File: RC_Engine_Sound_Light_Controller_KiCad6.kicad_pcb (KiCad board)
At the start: 2 copper layers, 87 x 40.3 mm, 44 parts, among them J1 RX, J10 RGB, J11 32, J12 CH1, J13 CH2, J14 CH3, J15 ESC, J16 CH4, J17 Brushed Motor output, J2 HeadL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

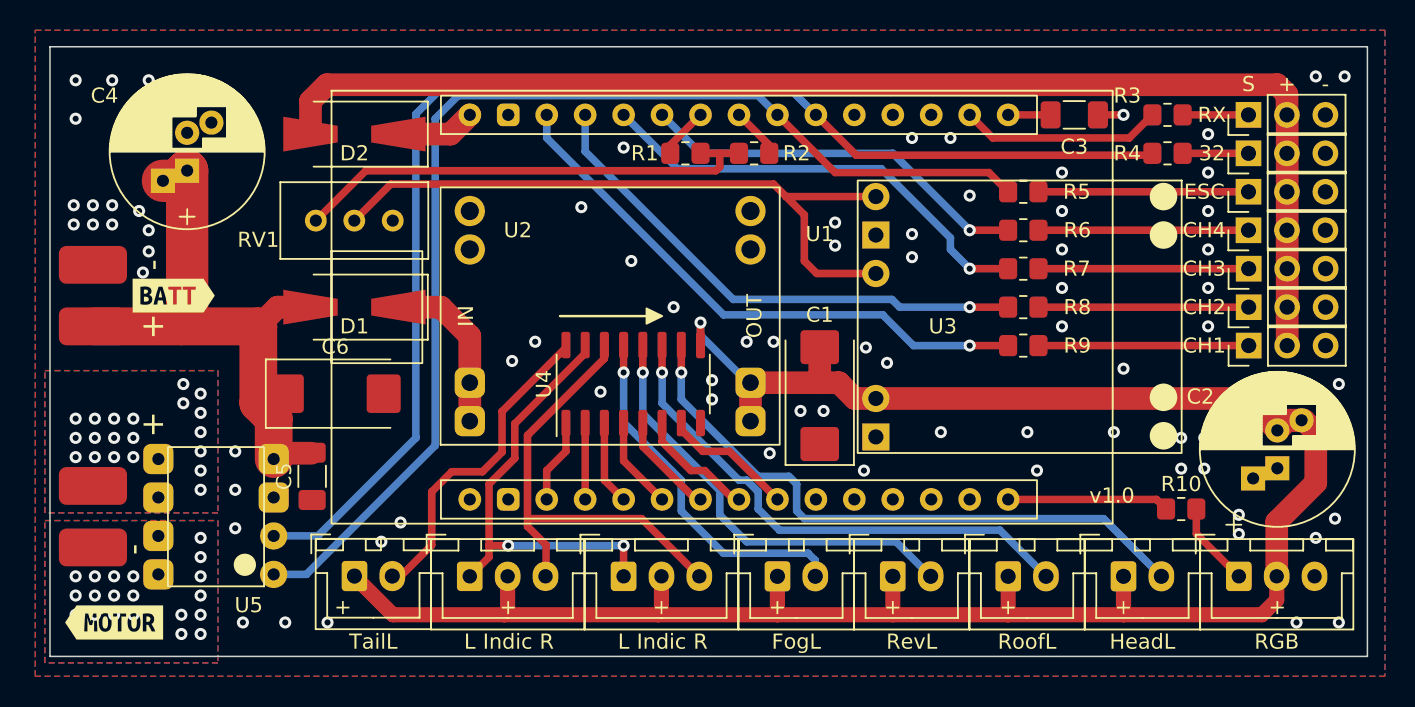
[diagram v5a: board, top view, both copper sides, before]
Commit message: Removed ESC and Pin 32 headers.
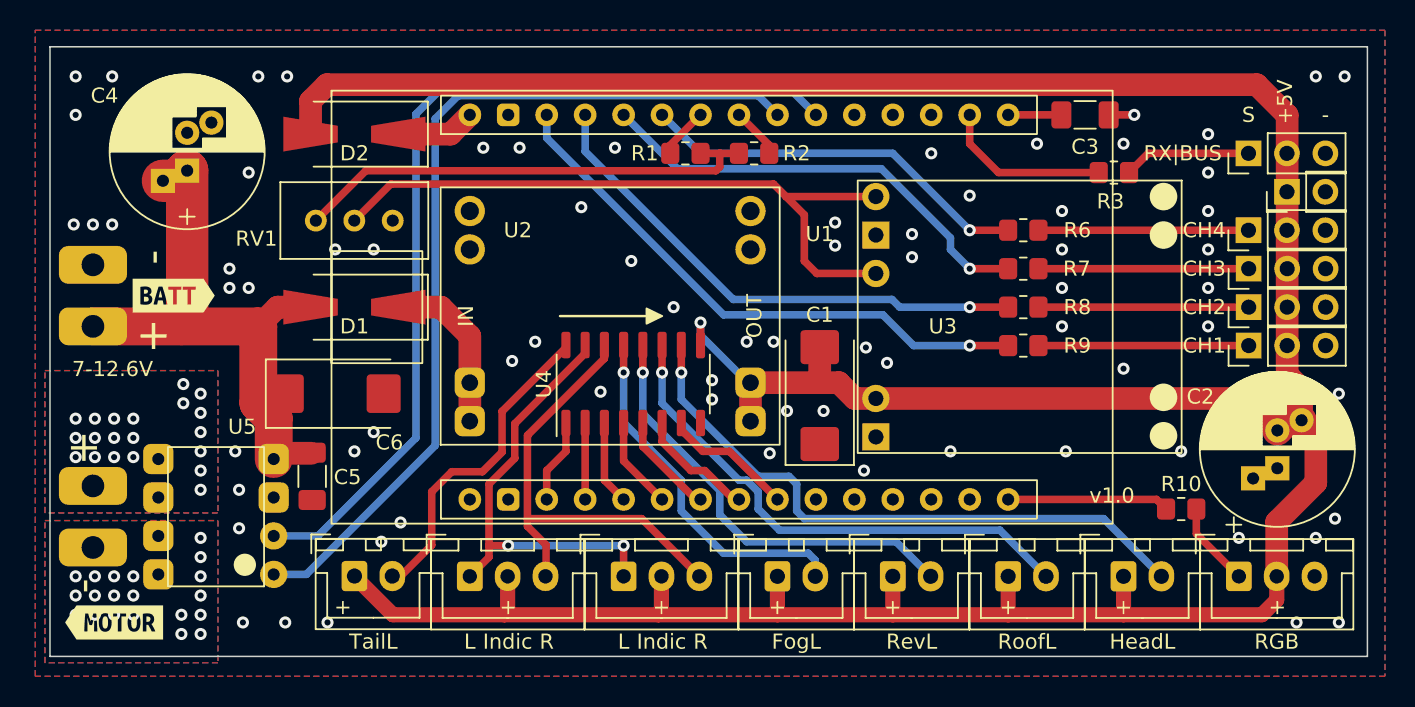
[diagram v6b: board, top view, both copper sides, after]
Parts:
- removed J11: 32, Connector_PinHeader_2.54mm:PinHeader_1x03_P2.54mm_Vertical
- removed J15: ESC, Connector_PinHeader_2.54mm:PinHeader_1x03_P2.54mm_Vertical
- removed R4: 180Ω, Resistor_SMD:R_0805_2012Metric_Pad1.20x1.40mm_HandSolder
- removed R5: 330Ω, Resistor_SMD:R_0805_2012Metric_Pad1.20x1.40mm_HandSolder
- added REF**: PinHeader_1x02_P2.54mm_Vertical, Connector_PinHeader_2.54mm:PinHeader_1x02_P2.54mm_Vertical, F.Cu at (146.7, 54.6)
- J1: value RX -> RX|BUS
- moved R3 5.20 mm to (135.3, 53.3)
- moved J1 2.54 mm to (144.1, 52.1)
- moved C3 0.71 mm to (133.3, 49.5)
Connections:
- D2 pad 2: VDD -> +5V
- J1 pad 2: VDD -> +5V
- J12 pad 2: VDD -> +5V
- J13 pad 2: VDD -> +5V
- J14 pad 2: VDD -> +5V
- J16 pad 2: VDD -> +5V
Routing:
- net +5V: track 144.2 -> 232.8 mm
- net VDD: track 84.0 -> 0.00 mm
- net D32: track 85.0 -> 61.8 mm
- net D33: track 76.9 -> 59.5 mm
- net /ESC: track 13.9 -> 0.00 mm
- net /PIN_32: track 4.35 -> 0.00 mm
- net /RX: track 4.35 -> 8.42 mm
- net D36: track 13.3 -> 11.2 mm
- net Net-(C3-Pad1): track 2.60 -> 3.52 mm
- net GND: vias 78 -> 75
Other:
- board text added: "+5V"
- board text added: "1:16 Small Crawler PCB v1.0 2022-05-23 by neo2001"
- board text added: "7-12.6V"
- board text removed: "Crawler PCB v1.0 2022-05-13 by neo2001"

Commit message: Rounded corners.
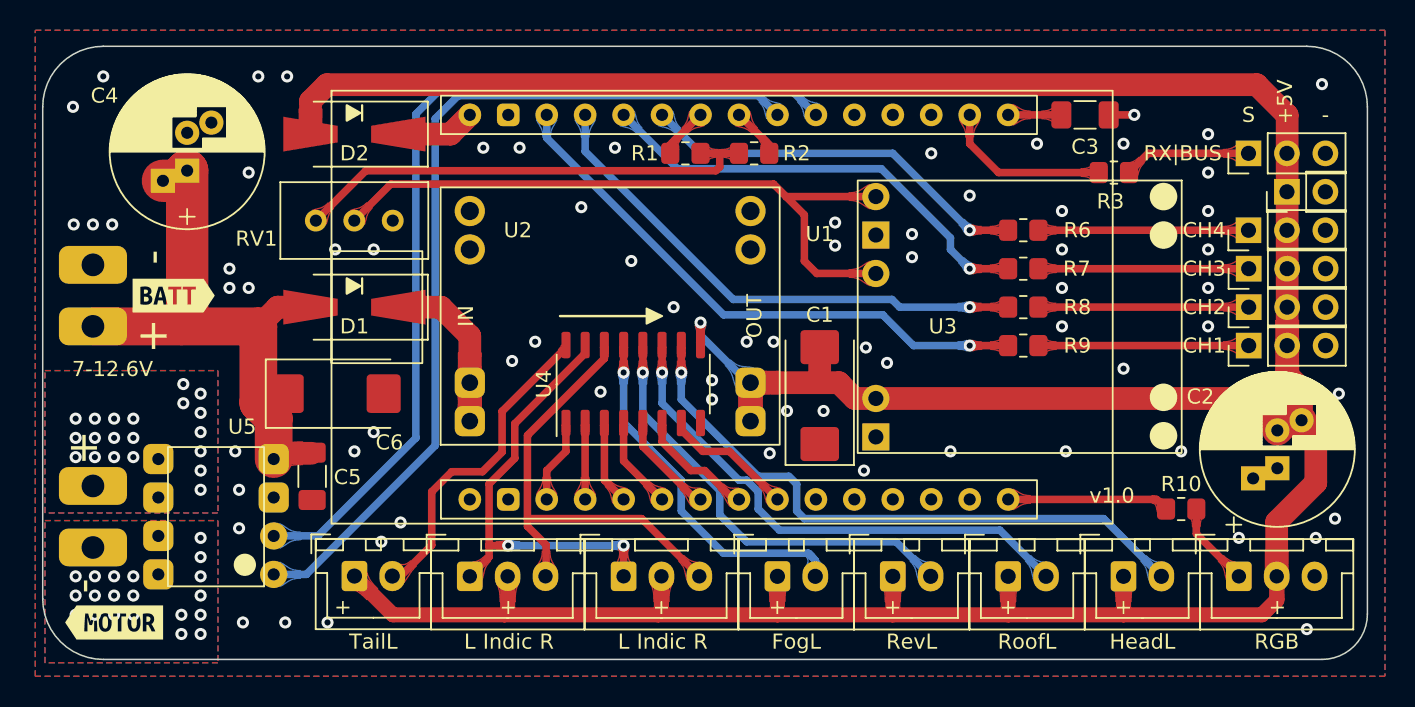
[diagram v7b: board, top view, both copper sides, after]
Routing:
- net GND: vias 75 -> 72
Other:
- board size 87 x 40.3 mm -> 87.5 x 40.5 mm

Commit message: Added voltage divider for battery voltage measurement. Renamed power nets.
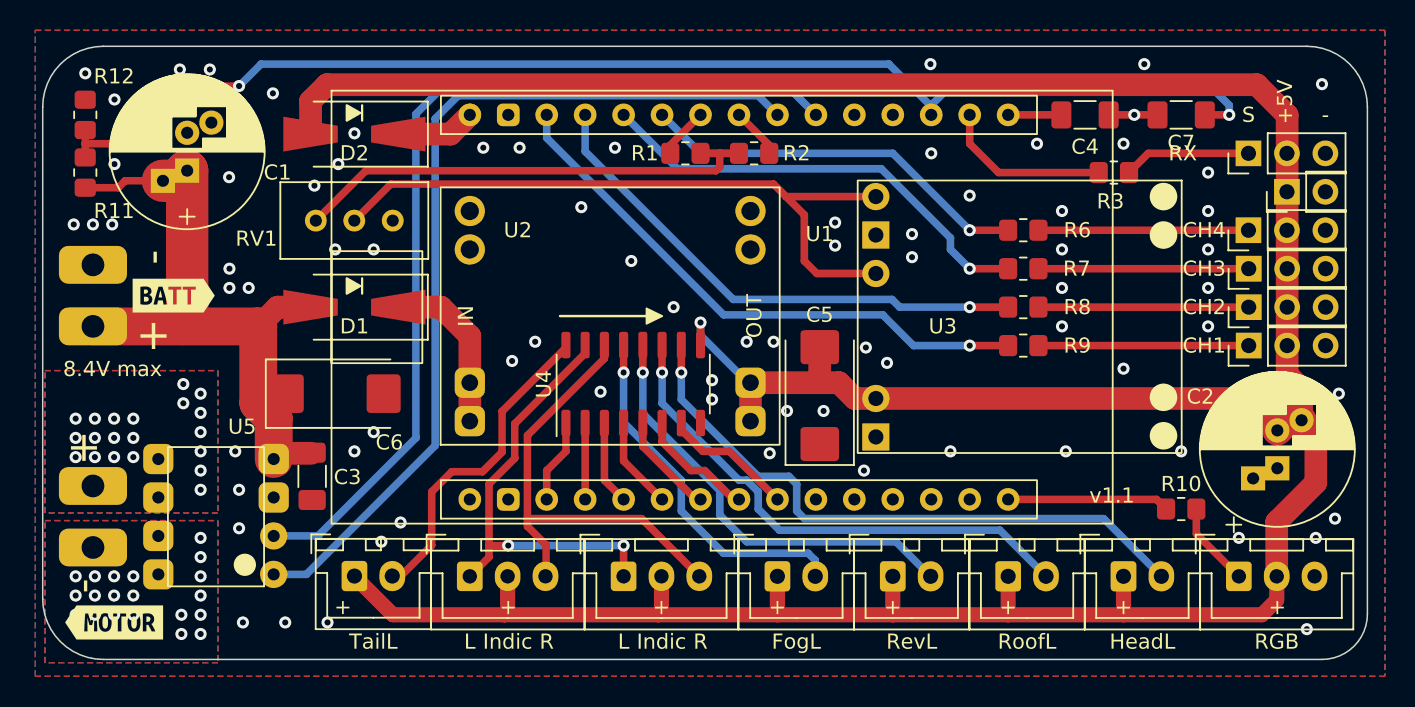
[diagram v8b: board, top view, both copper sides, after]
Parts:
- added C7: 100nF, Capacitor_SMD:C_1206_3216Metric_Pad1.33x1.80mm_HandSolder, F.Cu at (139.7, 49.5)
- added R11: 570kΩ, Resistor_SMD:R_0805_2012Metric_Pad1.20x1.40mm_HandSolder, F.Cu at (67.3, 53.3)
- added R12: 330kΩ, Resistor_SMD:R_0805_2012Metric_Pad1.20x1.40mm_HandSolder, F.Cu at (67.3, 49.5)
- J1: value RX|BUS -> RX
- renumbered C4 to C1, C5 to C3, C3 to C4, C1 to C5
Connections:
- net +10V renamed Net-(D1-Pad1)
- net +12V renamed +BATT
- net +5V renamed VCC
- C1 pad 2: GND -> -BATT
- C2 pad 1: GND -> -BATT
- C3 pad 1: GND -> -BATT
- C4 pad 2: GND -> -BATT
- C5 pad 1: GND -> -BATT
- C6 pad 2: GND -> -BATT
- J1 pad 3: GND -> -BATT
- J10 pad 3: GND -> -BATT
- J12 pad 3: GND -> -BATT
- J13 pad 3: GND -> -BATT
- J14 pad 3: GND -> -BATT
- J16 pad 3: GND -> -BATT
- J8 pad 2: GND -> -BATT
- RV1 pad 3: GND -> -BATT
- U1 pad 18: unconnected-(U1-Pad18) -> D39
- U1 pad 2: GND -> -BATT
- U1 pad 29: GND -> -BATT
- U2 pad 1: GND -> -BATT
- U2 pad 4: GND -> -BATT
- U2 pad 5: GND -> -BATT
- U2 pad 8: GND -> -BATT
- U3 pad 2: GND -> -BATT
- U3 pad 5: GND -> -BATT
- U4 pad 8: GND -> -BATT
- U5 pad 3: GND -> -BATT
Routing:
- net D39: track 0.00 -> 85.2 mm, vias 0 -> 2
- net +BATT: track 38.5 -> 43.8 mm
- net -BATT: track 0.00 -> 3.22 mm, vias 0 -> 79
- net GND: track 1.69 -> 0.00 mm, vias 72 -> 0
- added copper zone on B.Cu, net -BATT
- added copper zone on F.Cu, net -BATT
- removed copper zone on B.Cu, net GND
- removed copper zone on F.Cu, net GND
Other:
- board text added: "1:16 Small Crawler PCB v1.1 2022-05-23 by neo2001"
- board text added: "8.4V max"
- board text added: "v1.1"
- board text removed: "1:16 Small Crawler PCB v1.0 2022-05-23 by neo2001"
- board text removed: "7-12.6V"
- board text removed: "v1.0"
